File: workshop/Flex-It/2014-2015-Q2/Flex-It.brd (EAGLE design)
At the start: 84 x 80 mm, 14 parts, among them IC1 NE555D, Q1 MMBT2222A

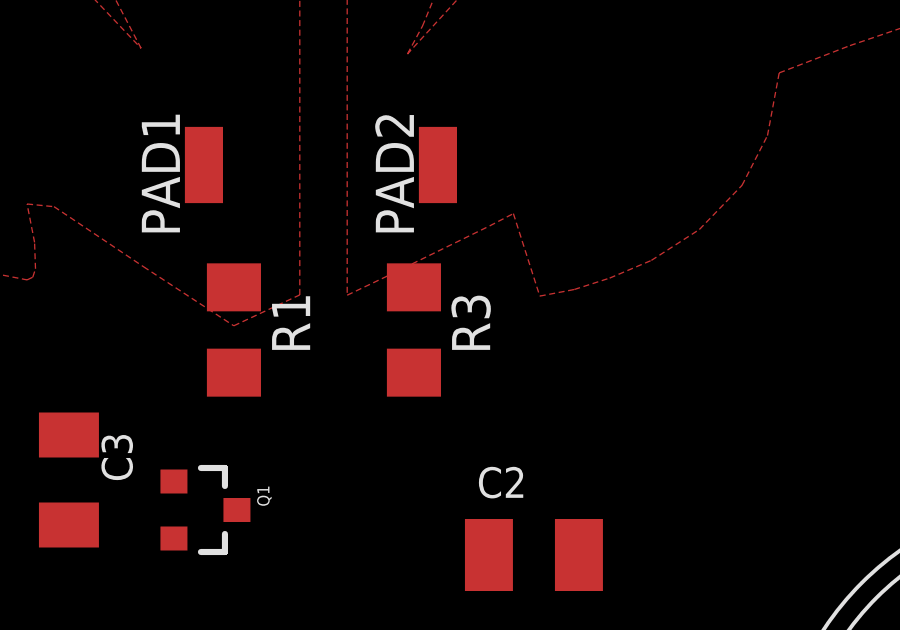
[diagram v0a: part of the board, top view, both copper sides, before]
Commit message: No thermals, larger isolation in polygons
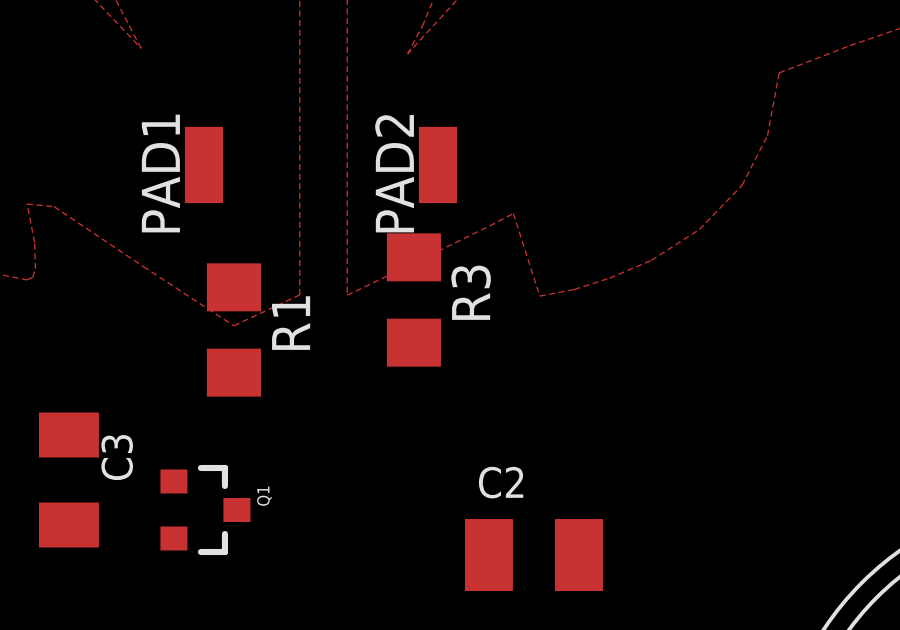
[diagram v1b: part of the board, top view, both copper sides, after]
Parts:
- moved R3 1.00 mm to (47.0, 37.0)
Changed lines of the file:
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@@
 <layer number="21" name="tPlace" color="7" fill="1" visible="yes" active="yes"/>
 <layer number="22" name="bPlace" color="7" fill="1" visible="yes" active="yes"/>
-<layer number="23" name="tOrigins" color="15" fill="1" visible="no" active="yes"/>
+<layer number="23" name="tOrigins" color="15" fill="1" visible="yes" active="yes"/>
 <layer number="24" name="bOrigins" color="15" fill="1" visible="yes" active="yes"/>
 <layer number="25" name="tNames" color="7" fill="1" visible="yes" active="yes"/>
@@
 <element name="R1" library="rcl" package="R1206" value="10k" x="41" y="36" rot="R270"/>
 <element name="R2" library="rcl" package="R1206" value="10" x="30" y="25"/>
-<element name="R3" library="rcl" package="R1206" value="270k" x="47" y="36" rot="R270"/>
+<element name="R3" library="rcl" package="R1206" value="270k" x="47" y="37" rot="R270"/>
 <element name="R4" library="rcl" package="R1206" value="10M" x="32" y="31" rot="R90"/>
 <element name="Q1" library="SparkFun-DiscreteSemi" package="SOT23-3" value="MMBT2222A" x="40" y="30" rot="R270">
@@
 <contactref element="R1" pad="1"/>
 <contactref element="PAD1" pad="1"/>
-<polygon width="0.254" layer="1" isolate="0.3048" rank="5">
+<polygon width="0.254" layer="1" isolate="0.3048" thermals="no" rank="5">
 <vertex x="43.185" y="79.04"/>
 <vertex x="33.795" y="79.04"/>
@@
 <vertex x="43.195" y="79.05"/>
 </polygon>
-<wire x1="41" y1="37.422" x2="40" y2="41.5" width="0" layer="19" extent="1-1"/>
-<wire x1="24.0734" y1="38.135" x2="40" y2="41.5" width="0" layer="19" extent="1-1"/>
+<wire x1="40" y1="41.5" x2="24.0734" y2="38.135" width="0" layer="19" extent="1-1"/>
 </signal>
 <signal name="TOUCH2">
 <contactref element="R3" pad="1"/>
 <contactref element="PAD2" pad="1"/>
-<polygon width="0.254" layer="1" isolate="0.254" rank="5">
+<polygon width="0.254" layer="1" isolate="0.254" thermals="no" rank="5">
 <vertex x="44.775" y="79.04"/>
 <vertex x="44.775" y="37.16"/>
@@
 <vertex x="44.895" y="79.04"/>
 </polygon>
-<wire x1="47" y1="37.422" x2="47.8" y2="41.5" width="0" layer="19" extent="1-1"/>
 </signal>
 <signal name="GND">
@@
 <contactref element="R2" pad="1"/>
 <contactref element="U$1" pad="2"/>
-<polygon width="0.254" layer="1" isolate="0.8128" orphans="yes" rank="6">
+<polygon width="0.254" layer="1" isolate="1.27" orphans="yes" thermals="no" rank="6">
 <vertex x="38.385" y="79.6"/>
 <vertex x="35.545" y="79.54"/>
@@
 <contactref element="IC1" pad="1"/>
 <contactref element="R5" pad="1"/>
-<wire x1="42" y1="16" x2="61.276978125" y2="22.30595" width="0" layer="19" extent="1-1"/>
-<wire x1="35.5" y1="29.5" x2="42" y2="16" width="0" layer="19" extent="1-1"/>
-<wire x1="32" y1="29.578" x2="35.5" y2="29.5" width="0" layer="19" extent="1-1"/>
-<wire x1="28.5" y1="29.5" x2="32" y2="29.578" width="0" layer="19" extent="1-1"/>
-<wire x1="28.578" y1="25" x2="28.5" y2="29.5" width="0" layer="19" extent="1-1"/>
-<wire x1="17.9266" y1="39.405" x2="28.5" y2="29.5" width="0" layer="19" extent="1-1"/>
 <wire x1="13.922" y1="42" x2="17.9266" y2="39.405" width="0" layer="19" extent="1-1"/>
-<wire x1="11.078" y1="42" x2="13.922" y2="42" width="0" layer="19" extent="1-1"/>
 </signal>
 <signal name="VCC">
@@
 <contactref element="IC1" pad="2"/>
 <contactref element="R3" pad="2"/>
-<wire x1="35.5" y1="32.5" x2="47" y2="34.578" width="0" layer="19" extent="1-1"/>
+<wire x1="35.5" y1="32.5" x2="47" y2="35.578" width="0" layer="19" extent="1-1"/>
 <wire x1="32" y1="32.422" x2="35.5" y2="32.5" width="0" layer="19" extent="1-1"/>
 <wire x1="24.0734" y1="36.865" x2="32" y2="32.422" width="0" layer="19" extent="1-1"/>
